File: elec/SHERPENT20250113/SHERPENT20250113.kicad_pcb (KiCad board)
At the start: 4 copper layers, 130.2 x 60.2 mm, 77 parts, among them J1 2137160001, J2 Conn_01x03_Socket, J3 Conn_01x03_Socket, Q1 NMOS, Q2 PMOS, Q3 NMOS, Q4 PMOS, SW2 SW_Push, U1 MCP73831T-2ACI_OT, U2 TPS61288LRQQR, U5 TPS7A2633DRVR, U6 AN034_ANTENNA, U7 ESP32-C3, U8 W25Q128JVS, Y1 40MHz

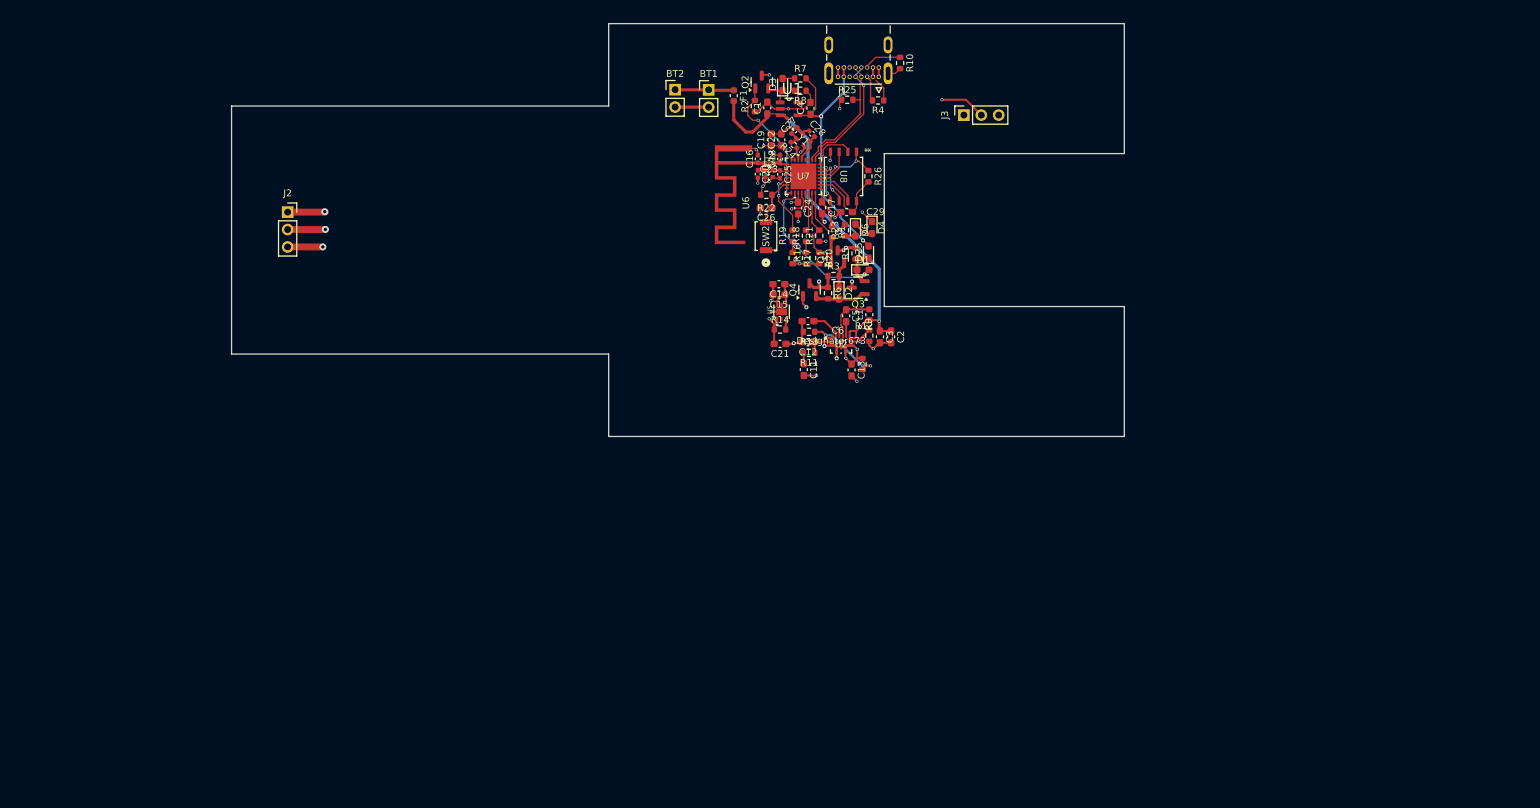
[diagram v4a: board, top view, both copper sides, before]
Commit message: Ajout de datasheet et changement de LDO
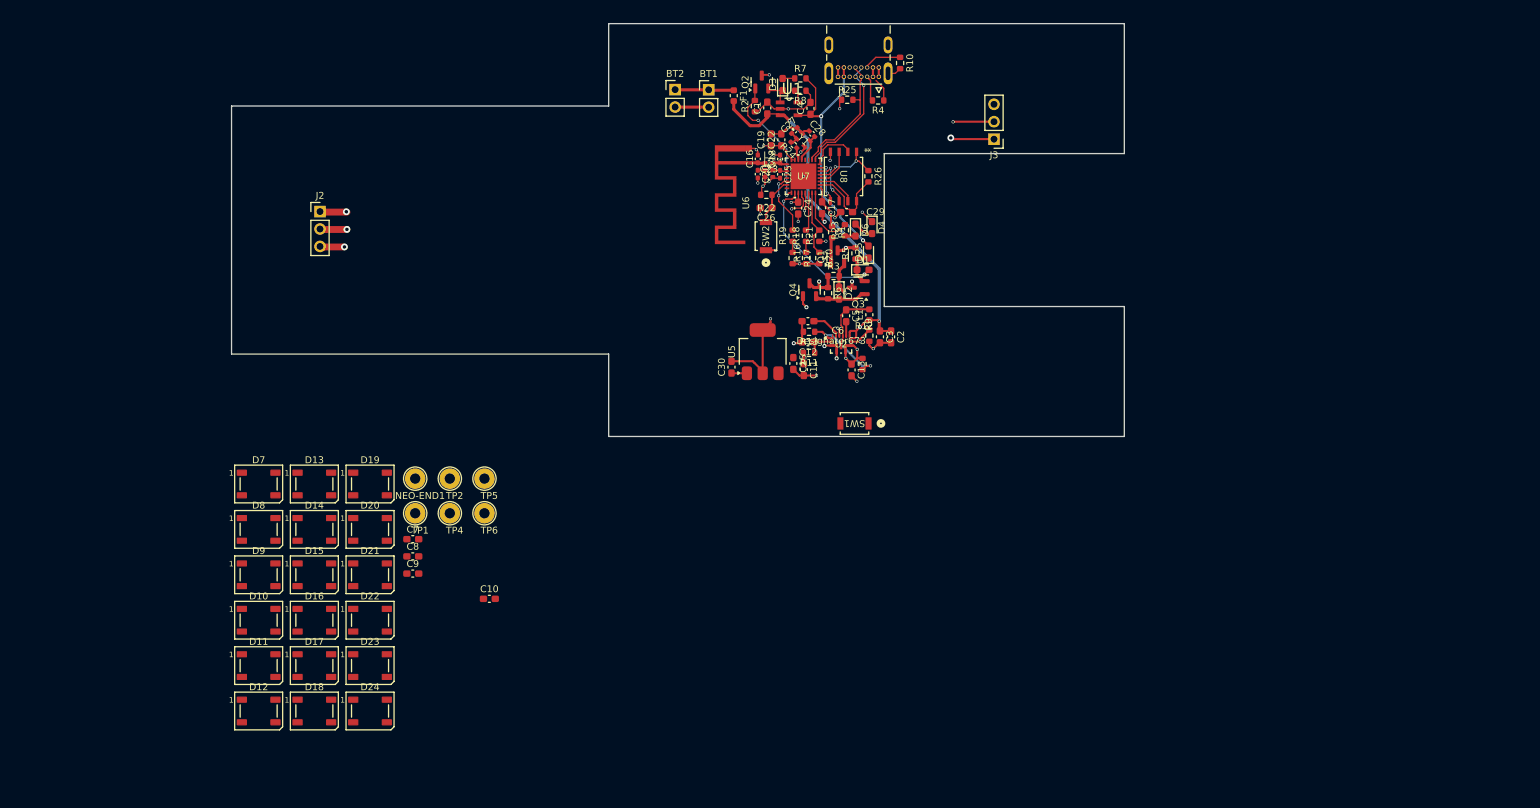
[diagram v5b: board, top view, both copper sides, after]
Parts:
- removed C14: TBD, Capacitor_SMD:C_0603_1608Metric_Pad1.08x0.95mm_HandSolder
- removed C21: 22u, Capacitor_SMD:C_0603_1608Metric_Pad1.08x0.95mm_HandSolder
- removed R14: 100k, Resistor_SMD:R_0603_1608Metric
- added C10: 1u, Capacitor_SMD:C_0603_1608Metric_Pad1.08x0.95mm_HandSolder, F.Cu at (114.5, 156.8)
- added C30: 4.7u, Capacitor_SMD:C_0603_1608Metric_Pad1.08x0.95mm_HandSolder, F.Cu at (149.8, 123.0)
- added C7: 100u, Capacitor_SMD:C_0603_1608Metric_Pad1.08x0.95mm_HandSolder, F.Cu at (103.4, 148.1)
- added C8: 100u, Capacitor_SMD:C_0603_1608Metric_Pad1.08x0.95mm_HandSolder, F.Cu at (103.4, 150.6)
- added C9: 1u, Capacitor_SMD:C_0603_1608Metric_Pad1.08x0.95mm_HandSolder, F.Cu at (103.4, 153.1)
- added D10: WS2812B, LED_SMD:LED_WS2812B_PLCC4_5.0x5.0mm_P3.2mm, F.Cu at (80.9, 159.9)
- added D11: WS2812B, LED_SMD:LED_WS2812B_PLCC4_5.0x5.0mm_P3.2mm, F.Cu at (80.9, 166.5)
- added D12: WS2812B, LED_SMD:LED_WS2812B_PLCC4_5.0x5.0mm_P3.2mm, F.Cu at (80.9, 173.1)
- added D13: WS2812B, LED_SMD:LED_WS2812B_PLCC4_5.0x5.0mm_P3.2mm, F.Cu at (89.0, 140.0)
- added D14: WS2812B, LED_SMD:LED_WS2812B_PLCC4_5.0x5.0mm_P3.2mm, F.Cu at (89.0, 146.6)
- added D15: WS2812B, LED_SMD:LED_WS2812B_PLCC4_5.0x5.0mm_P3.2mm, F.Cu at (89.0, 153.3)
- added D16: WS2812B, LED_SMD:LED_WS2812B_PLCC4_5.0x5.0mm_P3.2mm, F.Cu at (89.0, 159.9)
- added D17: WS2812B, LED_SMD:LED_WS2812B_PLCC4_5.0x5.0mm_P3.2mm, F.Cu at (89.0, 166.5)
- added D18: WS2812B, LED_SMD:LED_WS2812B_PLCC4_5.0x5.0mm_P3.2mm, F.Cu at (89.0, 173.1)
- added D19: WS2812B, LED_SMD:LED_WS2812B_PLCC4_5.0x5.0mm_P3.2mm, F.Cu at (97.1, 140.0)
- added D20: WS2812B, LED_SMD:LED_WS2812B_PLCC4_5.0x5.0mm_P3.2mm, F.Cu at (97.1, 146.6)
- added D21: WS2812B, LED_SMD:LED_WS2812B_PLCC4_5.0x5.0mm_P3.2mm, F.Cu at (97.1, 153.3)
- added D22: WS2812B, LED_SMD:LED_WS2812B_PLCC4_5.0x5.0mm_P3.2mm, F.Cu at (97.1, 159.9)
- added D23: WS2812B, LED_SMD:LED_WS2812B_PLCC4_5.0x5.0mm_P3.2mm, F.Cu at (97.1, 166.5)
- added D24: WS2812B, LED_SMD:LED_WS2812B_PLCC4_5.0x5.0mm_P3.2mm, F.Cu at (97.1, 173.1)
- added D7: WS2812B, LED_SMD:LED_WS2812B_PLCC4_5.0x5.0mm_P3.2mm, F.Cu at (80.9, 140.0)
- added D8: WS2812B, LED_SMD:LED_WS2812B_PLCC4_5.0x5.0mm_P3.2mm, F.Cu at (80.9, 146.6)
- added D9: WS2812B, LED_SMD:LED_WS2812B_PLCC4_5.0x5.0mm_P3.2mm, F.Cu at (80.9, 153.3)
- added NEO-END1: TestPoint, TestPoint:TestPoint_Loop_D2.54mm_Drill1.5mm_Beaded, F.Cu at (103.7, 139.2)
- added SW1: SW_Push, CS1213AGF160:SW_CS1213AG_CRS, F.Cu at (167.8, 131.2)
- added TP1: TestPoint, TestPoint:TestPoint_Loop_D2.54mm_Drill1.5mm_Beaded, F.Cu at (103.7, 144.3)
- added TP2: TestPoint, TestPoint:TestPoint_Loop_D2.54mm_Drill1.5mm_Beaded, F.Cu at (108.8, 139.2)
- added TP4: TestPoint, TestPoint:TestPoint_Loop_D2.54mm_Drill1.5mm_Beaded, F.Cu at (108.8, 144.3)
- added TP5: TestPoint, TestPoint:TestPoint_Loop_D2.54mm_Drill1.5mm_Beaded, F.Cu at (113.8, 139.2)
- added TP6: TestPoint, TestPoint:TestPoint_Loop_D2.54mm_Drill1.5mm_Beaded, F.Cu at (113.8, 144.3)
- C15: value 22u -> 100n
- J2, J3: footprint Connector_PinSocket_2.54mm:PinSocket_1x03_P2.54mm_Vertical -> Connector_PinHeader_2.54mm:PinHeader_1x03_P2.54mm_Vertical
- U5: value TPS7A2633DRVR -> LD1117S33TR_SOT223; footprint TPS7A2633DRVR:SON65P200X200X80-7N -> Package_TO_SOT_SMD:SOT-223-3_TabPin2
- moved C15 10.3 mm to (158.8, 122.5), turned to -90 degrees
- moved U5 6.44 mm to (154.4, 120.7)
- moved J3 5.62 mm to (188.1, 89.7), turned to 180 degrees
- moved J2 4.72 mm to (89.8, 100.3)
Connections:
- U5 pad 1: +3.3V -> GND
- U5 pad 2: unconnected-(U5-NC-Pad2) -> +3.3V
- U5 pad 3: Net-(U5-PG) -> /VDIODE
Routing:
- net +3.3V: track 57.5 -> 66.1 mm
- net GND: track 174.4 -> 165.9 mm, vias 28 -> 26
- net /Moteur1_PWM: track 82.9 -> 77.6 mm
- net /VDIODE: track 5.13 -> 0.00 mm
- net VBATT: track 73.3 -> 71.7 mm
- net Net-(U5-PG): track 1.61 -> 0.00 mm
- net Net-(D2-K): track 3.80 -> 4.97 mm, vias 0 -> 1
- net +9V: vias 3 -> 4

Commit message: Bouton placé
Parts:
- SW1: value SW_Push -> CT1102; footprint CS1213AGF160:SW_CS1213AG_CRS -> CT1102V3.15F100:CT1102V3.15F100
- moved C10 15.6 mm to (101.2, 165.0)
- moved C8 9.61 mm to (101.2, 160.0)
- moved NEO-END1 9.61 mm to (101.6, 148.6)
- moved TP1 9.61 mm to (101.6, 153.7)
- moved C7 9.61 mm to (101.2, 157.4)
- moved C9 9.61 mm to (101.2, 162.5)
- moved D10 9.61 mm to (78.8, 169.3)
- moved D11 9.61 mm to (78.8, 175.9)
- moved D12 9.61 mm to (78.8, 182.5)
- moved D13 9.61 mm to (86.9, 149.4)
- moved D14 9.61 mm to (86.9, 156.0)
- moved D15 9.61 mm to (86.9, 162.6)
- moved D16 9.61 mm to (86.9, 169.3)
- moved D17 9.61 mm to (86.9, 175.9)
- moved D18 9.61 mm to (86.9, 182.5)
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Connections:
- D11 pad 4: Net-(D11-DIN) -> Net-(D10-DOUT)
- D12 pad 4: Net-(D10-DOUT) -> Net-(D11-DOUT)
- D13 pad 4: Net-(D11-DOUT) -> Net-(D12-DOUT)
- D14 pad 4: Net-(D12-DOUT) -> Net-(D13-DOUT)
- D15 pad 2: Net-(D15-DOUT) -> /NEO_Row2
- D15 pad 4: Net-(D13-DOUT) -> Net-(D14-DOUT)
- D16 pad 4: Net-(D14-DOUT) -> /NEO_Row2
- D17 pad 4: Net-(D15-DOUT) -> Net-(D16-DOUT)
- D18 pad 4: Net-(D16-DOUT) -> Net-(D17-DOUT)
- D19 pad 4: Net-(D17-DOUT) -> Net-(D18-DOUT)
- D20 pad 4: Net-(D18-DOUT) -> Net-(D19-DOUT)
- D21 pad 4: Net-(D19-DOUT) -> Net-(D20-DOUT)
- D22 pad 4: Net-(D20-DOUT) -> Net-(D21-DOUT)
- D23 pad 2: /NEO_Row2 -> Net-(D23-DOUT)
- D23 pad 4: Net-(D21-DOUT) -> Net-(D22-DOUT)
- D24 pad 4: Net-(D22-DOUT) -> Net-(D23-DOUT)
- D8 pad 2: Net-(D10-DIN) -> Net-(D8-DOUT)
- D8 pad 4: /NEO_Row2 -> Net-(D7-DOUT)
- D9 pad 2: Net-(D11-DIN) -> Net-(D10-DIN)
- D9 pad 4: Net-(D7-DOUT) -> Net-(D8-DOUT)

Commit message: Tiens max have fun
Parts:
- removed NEO-END1, TP1, TP2, TP4, TP5, TP6: TestPoint, TestPoint:TestPoint_Loop_D2.54mm_Drill1.5mm_Beaded
- C10, C8, D10, D11, D12, D13, D15, D16, D18, D20, D21, D23, D8, D9, J2: moved to B.Cu
- moved D24 145.3 mm to (200.0, 82.0), turned to 180 degrees
- moved D23 140.8 mm to (200.0, 82.0), turned to 180 degrees
- moved D18 127.8 mm to (200.0, 123.0), turned to 180 degrees
- moved D22 121.8 mm to (180.0, 82.0), turned to 180 degrees
- moved D21 117.2 mm to (180.0, 82.0), turned to 180 degrees
- moved D19 108.3 mm to (200.0, 123.0), turned to 180 degrees
- moved D17 107.1 mm to (180.0, 123.0), turned to 180 degrees
- moved D16 104.0 mm to (180.0, 123.0), turned to 180 degrees
- moved D7 81.1 mm to (136.0, 92.0)
- moved D8 80.2 mm to (127.0, 92.0), turned to 180 degrees
- moved D20 79.8 mm to (136.0, 87.5), turned to 180 degrees
- moved D10 77.7 mm to (87.0, 92.0), turned to 180 degrees
- moved D15 77.3 mm to (147.0, 114.0), turned to 180 degrees
- moved D9 76.1 mm to (107.0, 92.0), turned to 180 degrees
- moved C10 75.7 mm to (95.0, 89.5), turned to 180 degrees
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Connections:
- D10 pad 1: unconnected-(D10-VDD-Pad1) -> +5V
- D11 pad 1: unconnected-(D11-VDD-Pad1) -> +5V
- D12 pad 1: unconnected-(D12-VDD-Pad1) -> +5V
- D13 pad 1: unconnected-(D13-VDD-Pad1) -> +5V
- D14 pad 1: unconnected-(D14-VDD-Pad1) -> +5V
- D15 pad 1: unconnected-(D15-VDD-Pad1) -> +5V
- D16 pad 1: unconnected-(D16-VDD-Pad1) -> +5V
- D17 pad 1: unconnected-(D17-VDD-Pad1) -> +5V
- D18 pad 1: unconnected-(D18-VDD-Pad1) -> +5V
- D19 pad 1: unconnected-(D19-VDD-Pad1) -> +5V
- D20 pad 1: unconnected-(D20-VDD-Pad1) -> +5V
- D21 pad 1: unconnected-(D21-VDD-Pad1) -> +5V
- D22 pad 1: unconnected-(D22-VDD-Pad1) -> +5V
- D23 pad 1: unconnected-(D23-VDD-Pad1) -> +5V
- D24 pad 1: unconnected-(D24-VDD-Pad1) -> +5V
- D7 pad 1: unconnected-(D7-VDD-Pad1) -> +5V
- D8 pad 1: unconnected-(D8-VDD-Pad1) -> +5V
- D9 pad 1: unconnected-(D9-VDD-Pad1) -> +5V
- J1 pad SH1: GND -> unconnected-(J1-SHIELD1-PadSH1)
- J1 pad SH2: GND -> unconnected-(J1-SHIELD2-PadSH2)
- J1 pad SH3: GND -> unconnected-(J1-SHIELD3-PadSH3)
- J1 pad SH4: GND -> unconnected-(J1-SHIELD4-PadSH4)
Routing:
- net +5V: track 0.00 -> 107.5 mm, vias 0 -> 4
- net GND: track 165.9 -> 122.6 mm, vias 26 -> 29
- net /NEOPX: track 0.00 -> 29.1 mm, vias 0 -> 2
- net Net-(D10-DIN): track 0.00 -> 28.2 mm
- net Net-(D8-DOUT): track 0.00 -> 27.8 mm
- net Net-(D10-DOUT): track 0.00 -> 20.7 mm
- net Net-(D12-DOUT): track 0.00 -> 16.5 mm
- net Net-(D11-DOUT): track 0.00 -> 16.5 mm
- net Net-(D7-DOUT): track 0.00 -> 10.4 mm, vias 0 -> 1
- net Net-(J1-CC2): track 5.62 -> 11.0 mm
- net +3.3V: track 66.1 -> 63.2 mm
- net +9V: track 149.7 -> 151.4 mm
- net /Moteur1_PWM: track 77.6 -> 78.6 mm

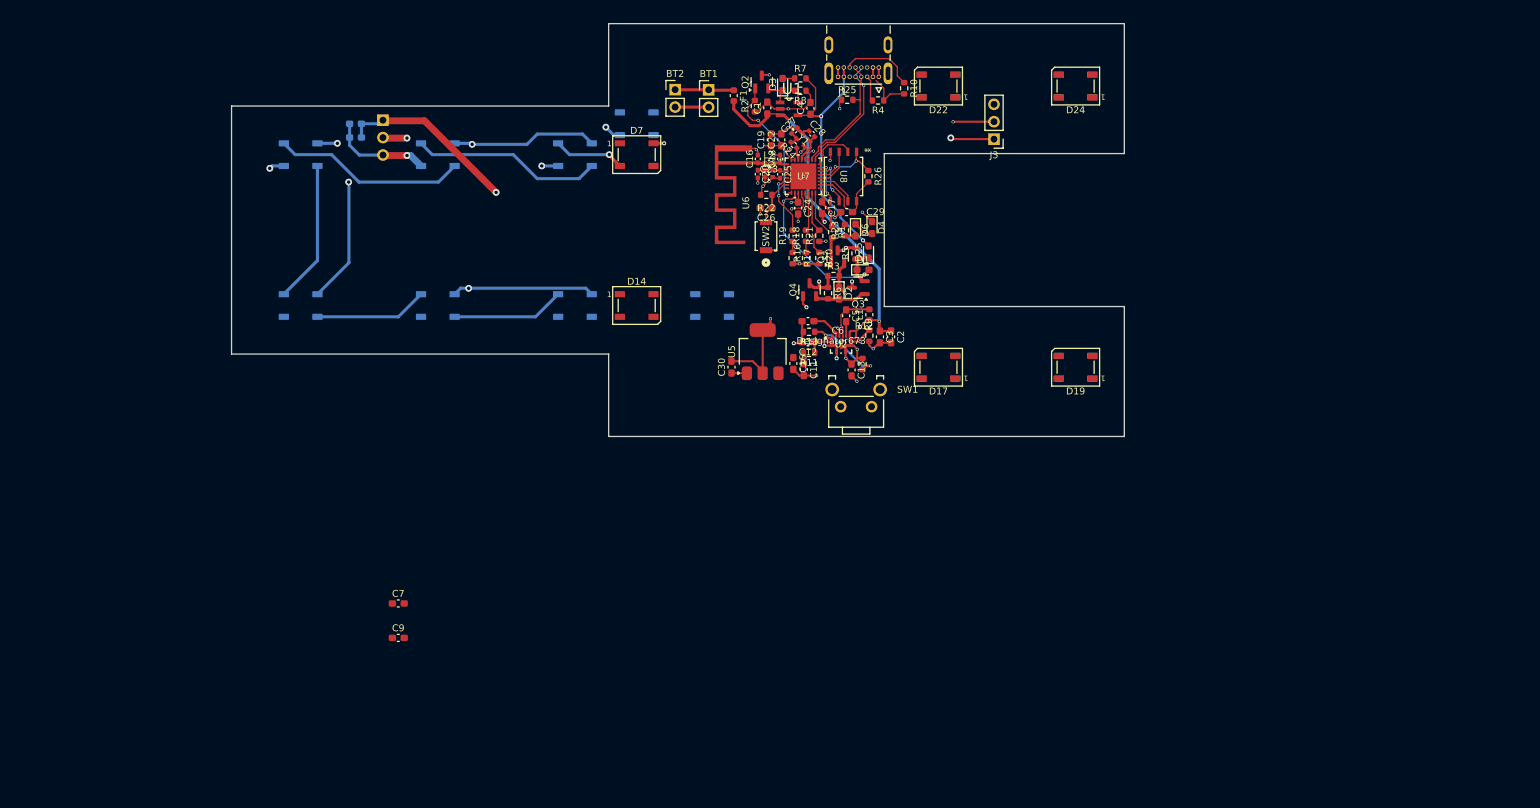
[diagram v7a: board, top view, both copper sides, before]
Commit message: Changement de place de l'ESP
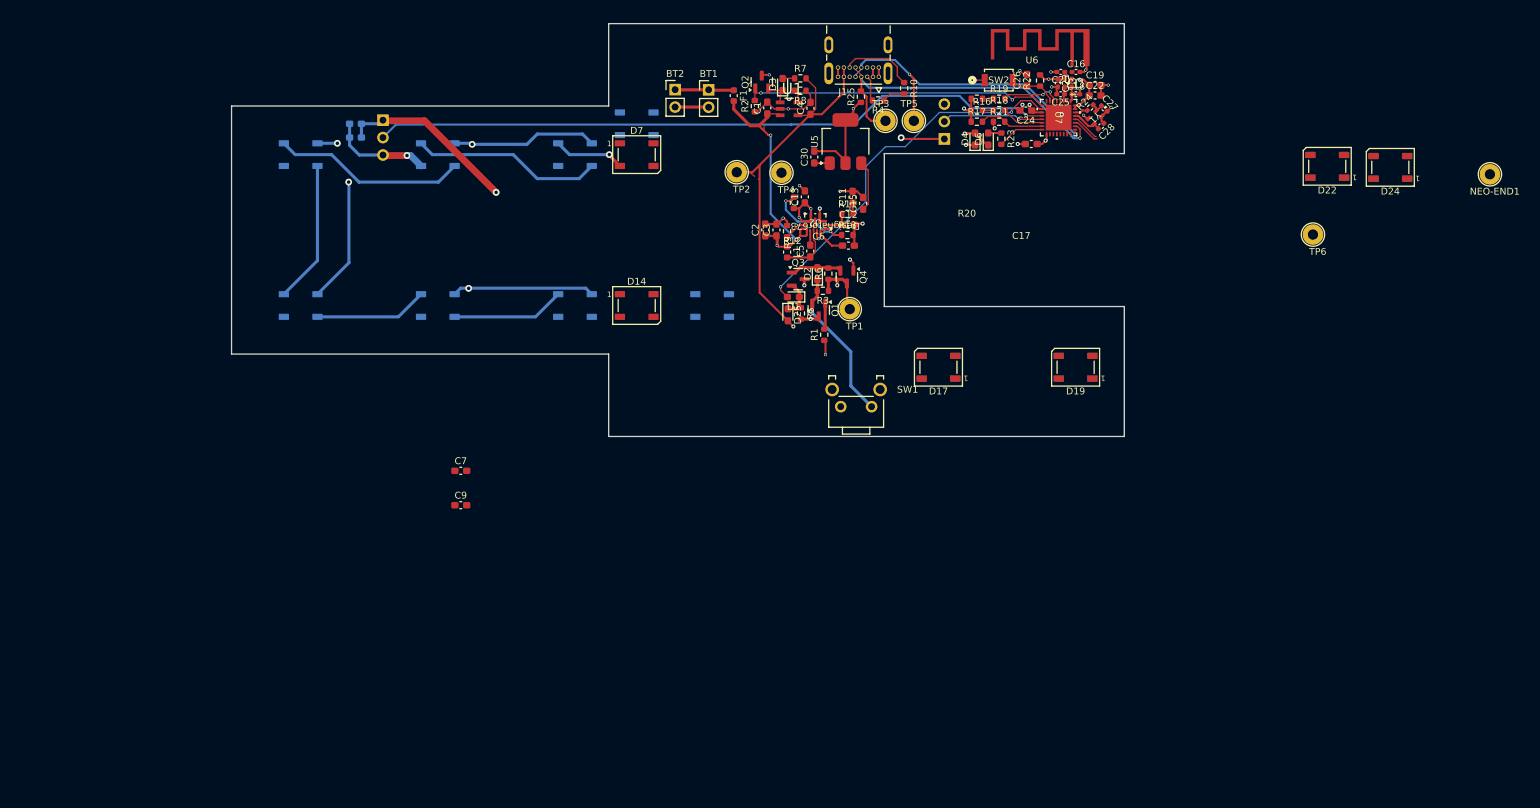
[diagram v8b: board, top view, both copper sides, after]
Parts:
- removed C29: 1u, Capacitor_SMD:C_0603_1608Metric_Pad1.08x0.95mm_HandSolder
- removed R26: 10k, Resistor_SMD:R_0603_1608Metric
- removed U8: W25Q128JVS, W25Q128JVSIQ:SOIC_128JVSIQ_WIN-L
- added NEO-END1: TestPoint, TestPoint:TestPoint_Loop_D2.54mm_Drill1.5mm_Beaded, F.Cu at (260.4, 94.9)
- added TP1: TestPoint, TestPoint:TestPoint_Loop_D2.54mm_Drill1.5mm_Beaded, F.Cu at (167.1, 114.5)
- added TP2: TestPoint, TestPoint:TestPoint_Loop_D2.54mm_Drill1.5mm_Beaded, F.Cu at (150.6, 94.6)
- added TP3: TestPoint, TestPoint:TestPoint_Loop_D2.54mm_Drill1.5mm_Beaded, F.Cu at (172.3, 87.1)
- added TP4: TestPoint, TestPoint:TestPoint_Loop_D2.54mm_Drill1.5mm_Beaded, F.Cu at (157.1, 94.6)
- added TP5: TestPoint, TestPoint:TestPoint_Loop_D2.54mm_Drill1.5mm_Beaded, F.Cu at (176.4, 87.1)
- added TP6: TestPoint, TestPoint:TestPoint_Loop_D2.54mm_Drill1.5mm_Beaded, F.Cu at (234.6, 103.7)
- J3: moved to B.Cu
- moved D21 57.9 mm to (236.7, 93.7)
- moved D22 57.9 mm to (236.7, 93.7)
- moved C16 48.1 mm to (200.1, 79.9), turned to 0 degrees
- moved C19 47.9 mm to (202.8, 81.9), turned to 0 degrees
- moved D23 47.4 mm to (245.9, 93.9)
- moved D24 47.4 mm to (245.9, 93.9)
- moved C20 46.6 mm to (197.8, 79.9), turned to 180 degrees
- moved C22 46.2 mm to (202.8, 83.4), turned to 0 degrees
- moved U6 45.9 mm to (194.4, 79.0), turned to 0 degrees
- moved L2 45.7 mm to (199.4, 81.6), turned to -90 degrees
- moved C27 45.3 mm to (204.2, 85.3), turned to -45 degrees
- moved L3 45.0 mm to (198.4, 81.6), turned to -90 degrees
- moved C23 44.3 mm to (197.4, 81.6), turned to -90 degrees
- moved C18 44.2 mm to (200.0, 83.2), turned to 0 degrees
- moved R24 43.5 mm to (202.1, 85.1), turned to 45 degrees
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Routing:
- net /StayOn: track 22.7 -> 55.0 mm
- net /USB_ESP32P: track 18.6 -> 49.1 mm, vias 0 -> 1
- net /USB_ESP32N: track 18.0 -> 45.8 mm, vias 1 -> 2
- net /VUSB: track 38.6 -> 64.3 mm, vias 2 -> 1
- net /CHARGE: track 19.7 -> 45.2 mm
- net /NEOPX: track 29.1 -> 4.10 mm, vias 2 -> 0
- net /Moteur2_PWM: track 38.3 -> 14.8 mm, vias 2 -> 1
- net /Moteur1_PWM: track 78.6 -> 99.8 mm, vias 2 -> 1
- net GND: track 122.6 -> 102.4 mm, vias 29 -> 25
- net Net-(D2-K): track 4.97 -> 22.6 mm
- net VBATT: track 71.7 -> 58.2 mm
- net /SQPI_VDD_ESP: track 12.8 -> 0.00 mm
- net +3.3V: track 63.2 -> 51.1 mm
- net /SQPI_SS_ESP: track 9.95 -> 0.00 mm, vias 2 -> 0
- net +9V: track 151.4 -> 143.7 mm, vias 4 -> 5
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- added copper zone on In2.Cu, net +5V
- added copper zone on F.Cu, net +9V
- added copper zone on F.Cu, net /VUSB
- added copper zone on F.Cu, net VBATT
